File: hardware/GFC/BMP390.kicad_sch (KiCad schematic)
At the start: 10 parts, among them U3 BMP390L

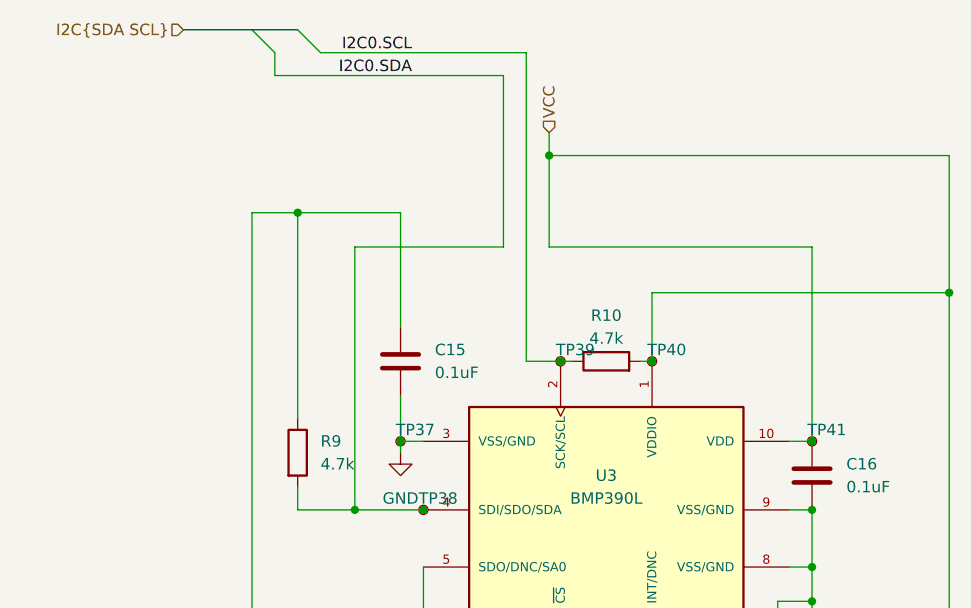
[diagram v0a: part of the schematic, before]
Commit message: Cleaning up the hardware directory
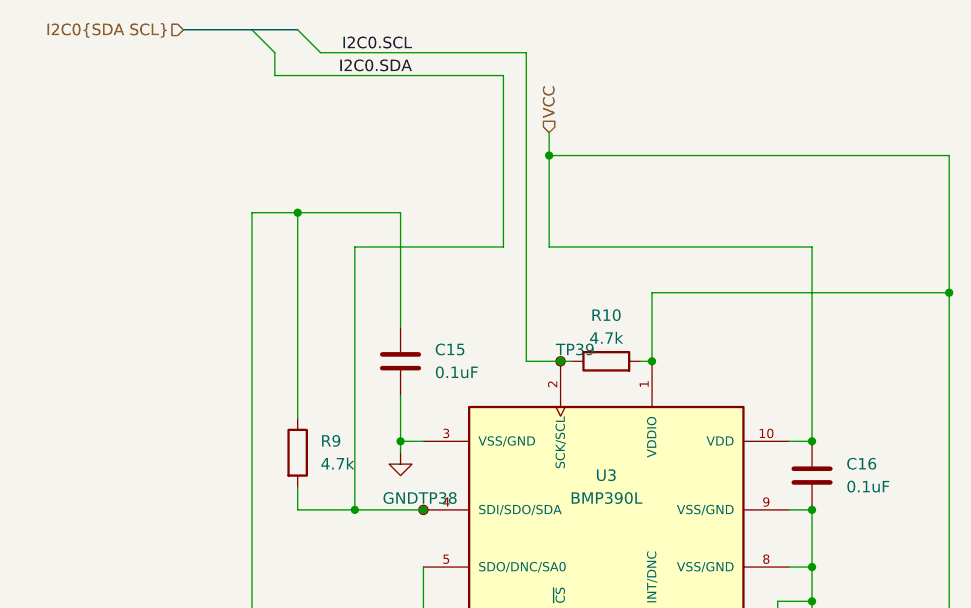
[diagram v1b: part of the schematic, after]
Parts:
- removed TP37, TP40, TP41: Test Point, TestPoint:TestPoint_Pad_D1.0mm, symbol Connector:TestPoint_Small
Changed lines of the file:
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@@
     (effects (font (size 1.27 1.27)) (justify left))
   )
-  (hierarchical_label "I2C{SDA SCL}" (shape input) (at 59.69 13.97 180)
+  (hierarchical_label "I2C0{SDA SCL}" (shape input) (at 59.69 13.97 180)
     (effects (font (size 1.27 1.27)) (justify right))
   )
@@
     )
     (property "Datasheet" "~" (id 3) (at 96.52 50.8 0)
-      (effects (font (size 1.27 1.27)) hide)
-    )
-    (pin "1")
-  )
-  (symbol (lib_id "Connector:TestPoint_Small") (at 111.76 50.8 0) (mirror y) (unit 1)
-    (in_bom yes) (on_board yes)
-    (property "Reference" "TP40" (id 0) (at 115.57 49.53 0)
-      (effects (font (size 1.27 1.27)) (justify left))
-    )
-    (property "Value" "Test Point" (id 1) (at 110.49 52.0699 0)
-      (effects (font (size 1.27 1.27)) (justify left) hide)
-    )
-    (property "Footprint" "TestPoint:TestPoint_Pad_D1.0mm" (id 2) (at 106.68 50.8 0)
-      (effects (font (size 1.27 1.27)) hide)
-    )
-    (property "Datasheet" "~" (id 3) (at 106.68 50.8 0)
       (effects (font (size 1.27 1.27)) hide)
     )
@@
     (pin "1")
   )
-  (symbol (lib_id "Connector:TestPoint_Small") (at 129.54 59.69 0) (mirror y) (unit 1)
-    (in_bom yes) (on_board yes)
-    (property "Reference" "TP41" (id 0) (at 133.35 58.42 0)
-      (effects (font (size 1.27 1.27)) (justify left))
-    )
-    (property "Value" "Test Point" (id 1) (at 128.27 60.9599 0)
-      (effects (font (size 1.27 1.27)) (justify left) hide)
-    )
-    (property "Footprint" "TestPoint:TestPoint_Pad_D1.0mm" (id 2) (at 124.46 59.69 0)
-      (effects (font (size 1.27 1.27)) hide)
-    )
-    (property "Datasheet" "~" (id 3) (at 124.46 59.69 0)
-      (effects (font (size 1.27 1.27)) hide)
-    )
-    (pin "1")
-  )
   (symbol (lib_id "Device:R") (at 106.68 50.8 90) (unit 1)
     (in_bom yes) (on_board yes)
@@
     (pin "2")
   )
-  (symbol (lib_id "Connector:TestPoint_Small") (at 83.82 59.69 0) (mirror y) (unit 1)
-    (in_bom yes) (on_board yes)
-    (property "Reference" "TP37" (id 0) (at 87.63 58.42 0)
-      (effects (font (size 1.27 1.27)) (justify left))
-    )
-    (property "Value" "Test Point" (id 1) (at 82.55 60.9599 0)
-      (effects (font (size 1.27 1.27)) (justify left) hide)
-    )
-    (property "Footprint" "TestPoint:TestPoint_Pad_D1.0mm" (id 2) (at 78.74 59.69 0)
-      (effects (font (size 1.27 1.27)) hide)
-    )
-    (property "Datasheet" "~" (id 3) (at 78.74 59.69 0)
-      (effects (font (size 1.27 1.27)) hide)
-    )
-    (pin "1")
-  )
   (symbol (lib_id "BMP390L:BMP390L") (at 106.68 68.58 0) (unit 1)

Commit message: PCB Prototype
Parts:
- added C19, C21: 0.1uF, Capacitor_SMD:C_0603_1608Metric_Pad1.08x0.95mm_HandSolder, symbol Device:C
- added J3: Conn_01x05_Male, Connector_PinHeader_2.54mm:PinHeader_1x05_P2.54mm_Horizontal, symbol Connector:Conn_01x05_Male
- added R12, R13: 4.7k, Resistor_SMD:R_0603_1608Metric_Pad0.98x0.95mm_HandSolder, symbol Device:R
- added U7: BME280, PSON65P250X250X100-8N, symbol BME280:BME280
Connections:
- net GND: now also C19.1, C21.2, J3.3 (Pin_3), U7.1 (GND), U7.5 (SDO), U7.7 (GND)
- new net SCL: J3.5 (Pin_5), R13.1, U7.4 (SCK)
- new net SDA: J3.4 (Pin_4), R12.1, U7.3 (SDI)
- new net VDD: C19.2, J3.1 (Pin_1), U7.8 (VDD)
- new net VDDF: C21.1, J3.2 (Pin_2), R12.2, R13.2, U7.2 (CSB), U7.6 (VDDIO)
